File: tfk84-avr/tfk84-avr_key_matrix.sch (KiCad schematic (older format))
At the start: 168 parts

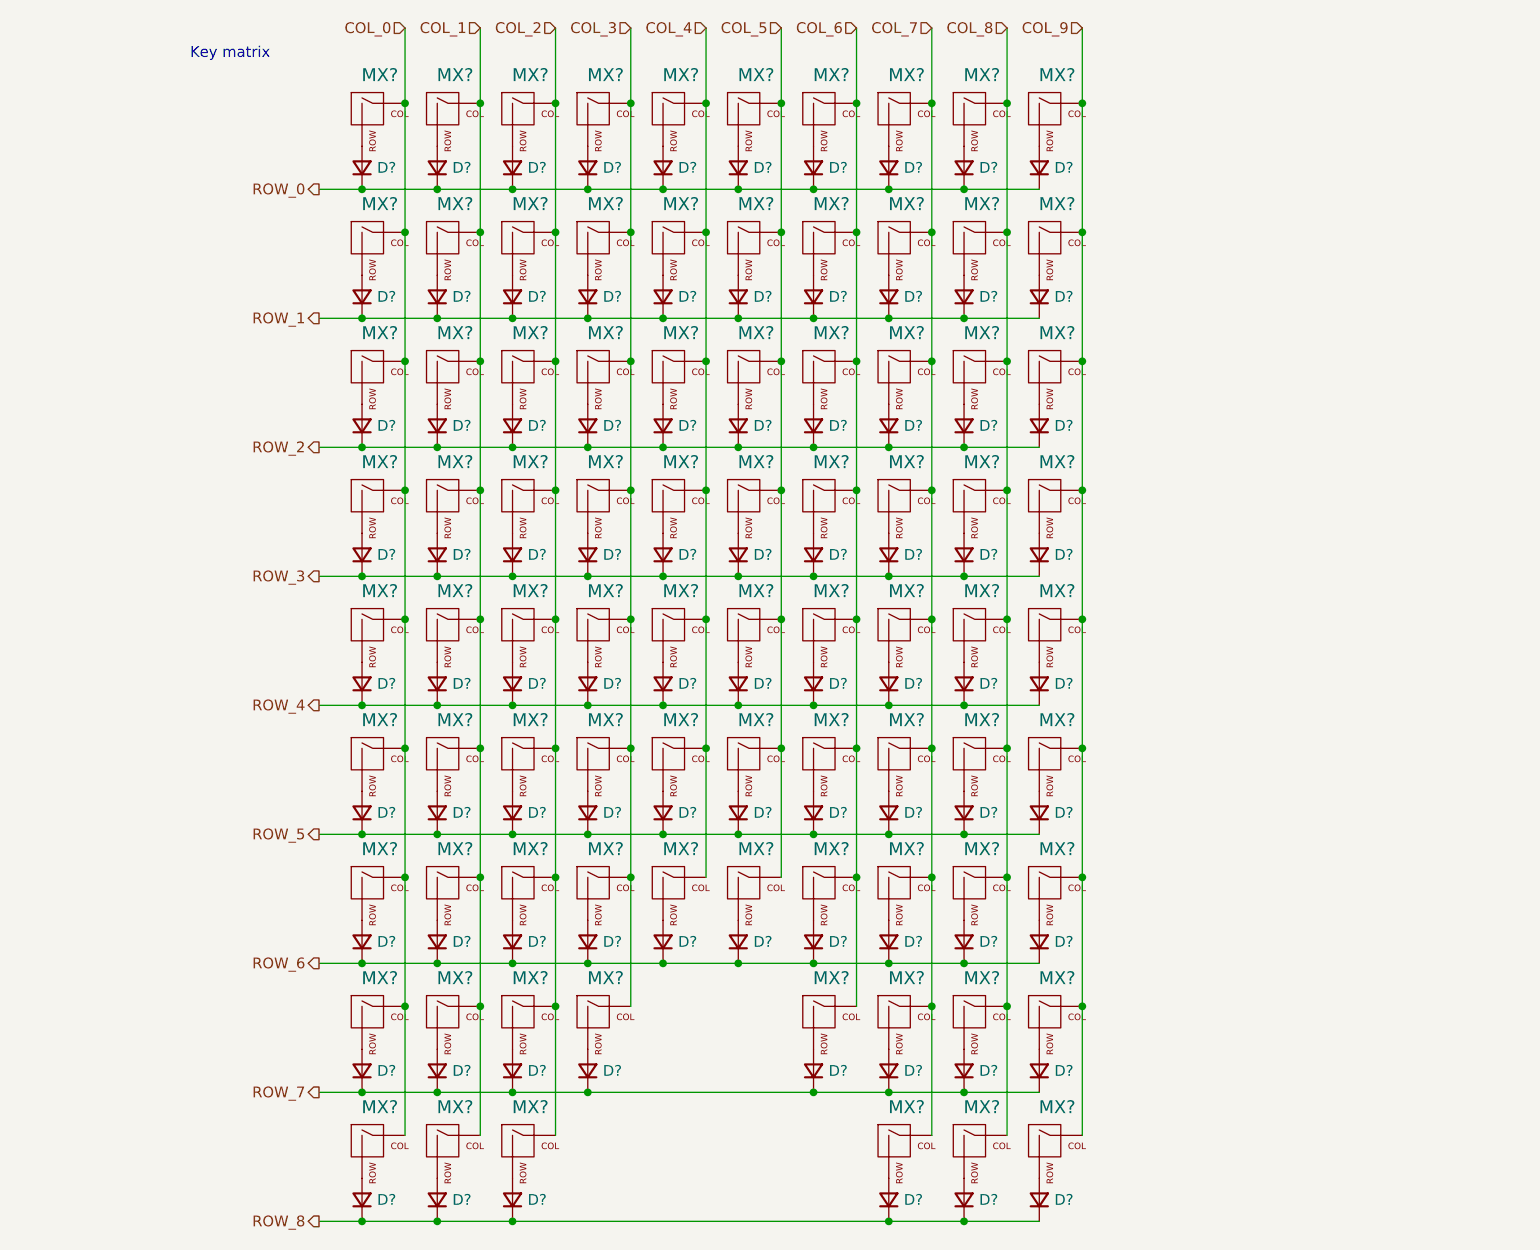
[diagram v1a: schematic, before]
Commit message: Change key matrix to 12x7
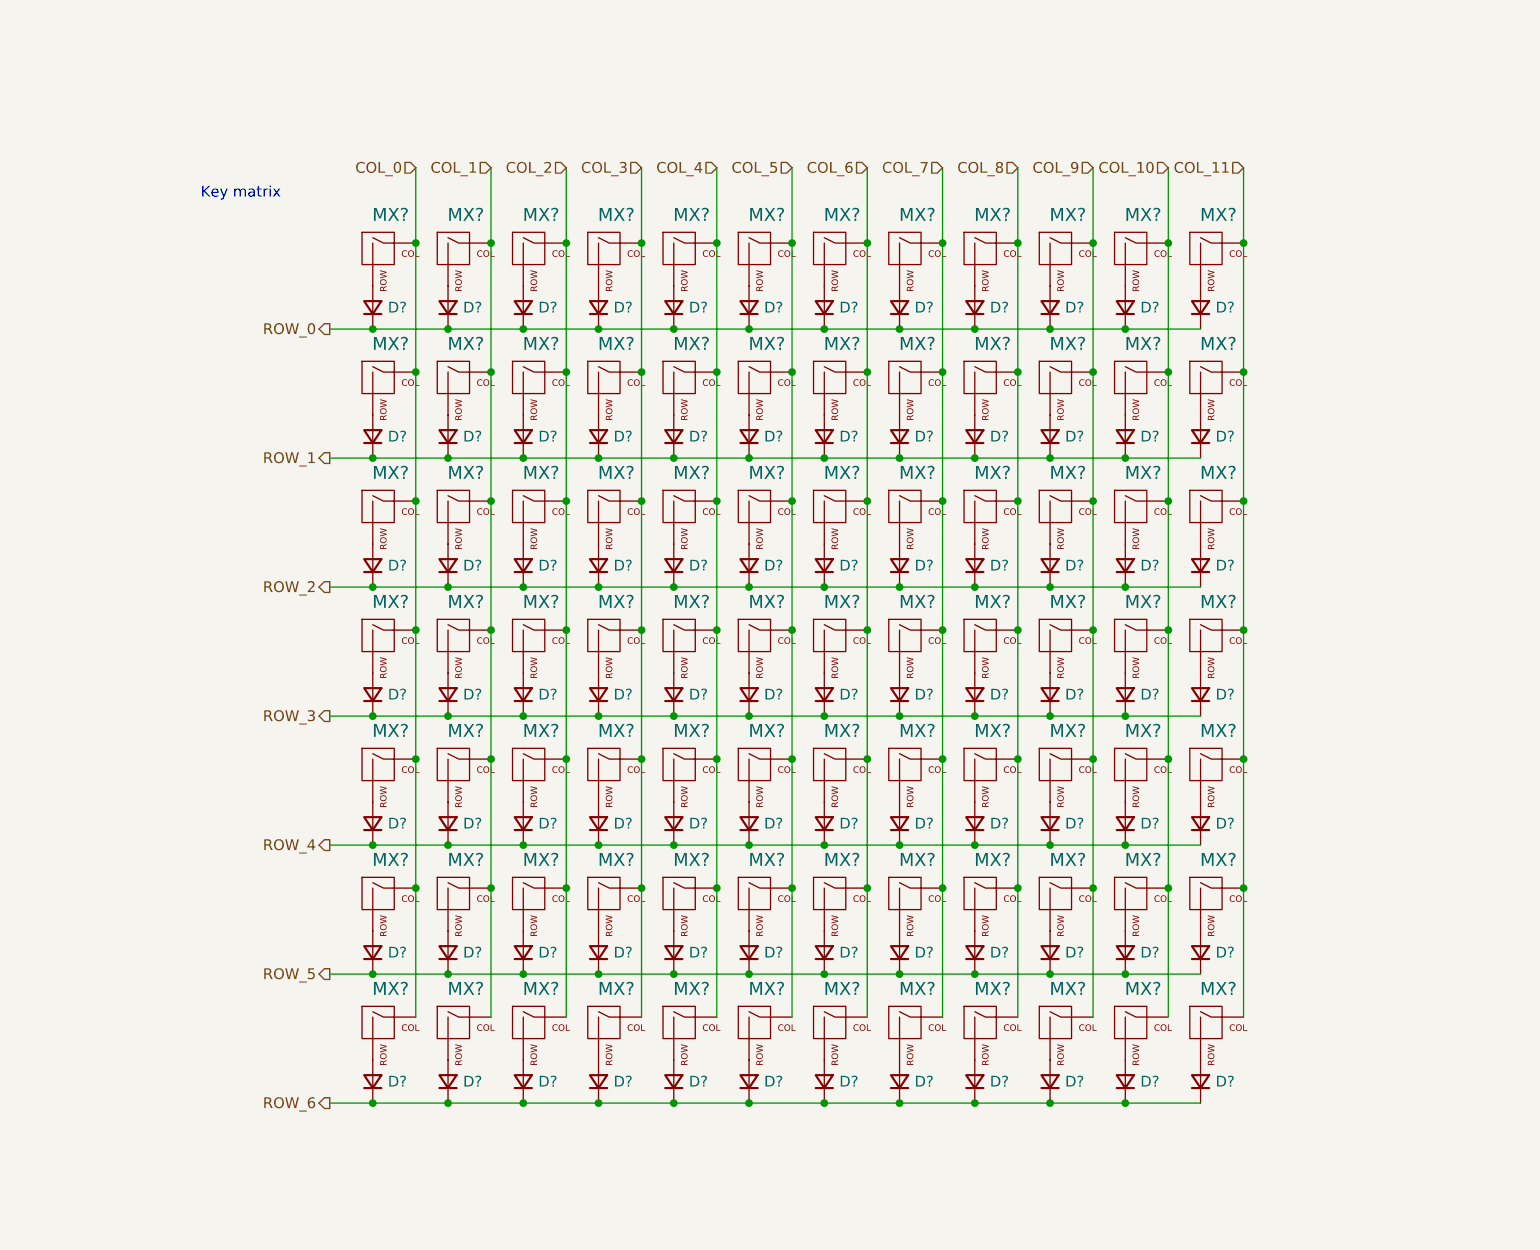
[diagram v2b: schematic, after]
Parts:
- removed D? (x14): D_Small, symbol Device:D_Small
- removed MX? (x14): MX-NoLED, symbol MX_Alps_Hybrid:MX-NoLED
- added D? (x14): D_Small, symbol Device:D_Small
- added MX? (x14): MX-NoLED, symbol MX_Alps_Hybrid:MX-NoLED
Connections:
- net ROW_0: now also D?.1 (K), D?.1 (K)
- net ROW_1: now also D?.1 (K), D?.1 (K)
- net ROW_2: now also D?.1 (K), D?.1 (K)
- net ROW_3: now also D?.1 (K), D?.1 (K)
- net ROW_4: now also D?.1 (K), D?.1 (K)
- net ROW_5: now also D?.1 (K), D?.1 (K)
- net ROW_6: now also D?.1 (K), D?.1 (K)
- new net: D?.2 (A), MX?.2 (ROW) (x14)
- new net COL_10: MX?.1 (COL), MX?.1 (COL), MX?.1 (COL), MX?.1 (COL), MX?.1 (COL), MX?.1 (COL), MX?.1 (COL)
- new net COL_11: MX?.1 (COL), MX?.1 (COL), MX?.1 (COL), MX?.1 (COL), MX?.1 (COL), MX?.1 (COL), MX?.1 (COL)
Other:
- moved on the sheet: D?, MX?

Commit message: Continue schematic
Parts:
- added H?: LShift stabilizer, symbol Mechanical:MountingHole
- added H?: Enter stabilizer, symbol Mechanical:MountingHole
- added H?: Backspace stabilizer, symbol Mechanical:MountingHole
- added H?: Space stabilizer, symbol Mechanical:MountingHole
- gave numbers to parts that had none: 168

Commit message: Begin PCB
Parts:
- D100, D101, D102, D103, D104, D105, D106, D107, D108, D109, D110, D111, D112, D113, D114, D115, D116, D117, D118, D119, D120, D121, D122, D123, D124, D125, D126, D127, D128, D129, D130, D131, D132, D133, D134, D135, D136, D137, D138, D139, D140, D141, D142, D143, D144, D145, D146, D147, D148, D149, D150, D151, D152, D153, D154, D155, D156, D157, D158, D159, D160, D161, D162, D163, D164, D165, D166, D167, D168, D169, D170, D171, D172, D173, D174, D175, D176, D177, D178, D179, D180, D181, D182, D183: footprint (none) -> Diode_SMD:D_SOD-123
- H5, H6, H7: renamed from H?; footprint (none) -> Mounting_Keyboard_Stabilizer:Stabilizer_Cherry_MX_2u_CrtYd
- H8: renamed from H?; footprint (none) -> Mounting_Keyboard_Stabilizer:Stabilizer_Cherry_MX_6.25u
- MX1, MX10, MX11, MX12, MX14, MX15, MX16, MX17, MX18, MX19, MX2, MX20, MX21, MX24, MX26, MX27, MX28, MX29, MX3, MX30, MX31, MX32, MX33, MX34, MX36, MX38, MX39, MX4, MX40, MX41, MX42, MX43, MX44, MX45, MX46, MX47, MX48, MX5, MX50, MX51, MX52, MX53, MX54, MX55, MX56, MX57, MX58, MX6, MX60, MX62, MX63, MX64, MX65, MX66, MX67, MX68, MX69, MX7, MX70, MX71, MX72, MX74, MX75, MX76, MX78, MX79, MX8, MX80, MX81, MX82, MX83, MX84, MX9: footprint (none) -> Switch_Keyboard_Kailh:SW_Hotswap_Kailh_1.00u_NoFrontSilk
- MX13, MX23: footprint (none) -> Switch_Keyboard_Kailh:SW_Hotswap_Kailh_1.50u
- MX22: footprint (none) -> Switch_Keyboard_Kailh:SW_Hotswap_Kailh_2.00u_NoFrontSilk
- MX25, MX59: footprint (none) -> Switch_Keyboard_Kailh:SW_Hotswap_Kailh_1.75u
- MX35, MX37: footprint (none) -> Switch_Keyboard_Kailh:SW_Hotswap_Kailh_2.25u
- MX49, MX61, MX73: footprint (none) -> Switch_Keyboard_Kailh:SW_Hotswap_Kailh_1.25u
- MX77: footprint (none) -> Switch_Keyboard_Kailh:SW_Hotswap_Kailh_6.25u
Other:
- moved on the sheet: H7, H8

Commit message: Add mounting holes for XD84 and KBD75V2 cases
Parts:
- renumbered H5 to H18, H6 to H19, H7 to H20, H8 to H21
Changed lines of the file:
@@
 P 3400 3550
 AR Path="/610B766F" Ref="H?"  Part="1"
-AR Path="/601C3315/610B766F" Ref="H7"  Part="1"
-F 0 "H7" H 3300 3504 50  0000 R CNN
+AR Path="/601C3315/610B766F" Ref="H20"  Part="1"
+F 0 "H20" H 3300 3504 50  0000 R CNN
 F 1 "LShift stabilizer" H 3300 3595 50  0000 R CNN
 F 2 "Mounting_Keyboard_Stabilizer:Stabilizer_Cherry_MX_2u_CrtYd" H 3400 3550 50  0001 C CNN
@@
 P 8400 2950
 AR Path="/610B7675" Ref="H?"  Part="1"
-AR Path="/601C3315/610B7675" Ref="H6"  Part="1"
-F 0 "H6" H 8500 2996 50  0000 L CNN
+AR Path="/601C3315/610B7675" Ref="H19"  Part="1"
+F 0 "H19" H 8500 2996 50  0000 L CNN
 F 1 "Enter stabilizer" H 8500 2905 50  0000 L CNN
 F 2 "Mounting_Keyboard_Stabilizer:Stabilizer_Cherry_MX_2u_CrtYd" H 8400 2950 50  0001 C CNN
@@
 P 8400 2350
 AR Path="/610B767B" Ref="H?"  Part="1"
-AR Path="/601C3315/610B767B" Ref="H5"  Part="1"
-F 0 "H5" H 8500 2396 50  0000 L CNN
+AR Path="/601C3315/610B767B" Ref="H18"  Part="1"
+F 0 "H18" H 8500 2396 50  0000 L CNN
 F 1 "Backspace stabilizer" H 8500 2305 50  0000 L CNN
 F 2 "Mounting_Keyboard_Stabilizer:Stabilizer_Cherry_MX_2u_CrtYd" H 8400 2350 50  0001 C CNN
@@
 P 5550 6000
 AR Path="/610B7681" Ref="H?"  Part="1"
-AR Path="/601C3315/610B7681" Ref="H8"  Part="1"
-F 0 "H8" H 5650 6046 50  0000 L CNN
+AR Path="/601C3315/610B7681" Ref="H21"  Part="1"
+F 0 "H21" H 5650 6046 50  0000 L CNN
 F 1 "Space stabilizer" H 5650 5955 50  0000 L CNN
 F 2 "Mounting_Keyboard_Stabilizer:Stabilizer_Cherry_MX_6.25u" H 5550 6000 50  0001 C CNN

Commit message: Tweak holes
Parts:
- MX14: footprint Switch_Keyboard_Kailh:SW_Hotswap_Kailh_1.00u_NoFrontSilk -> random-keyboard-parts:SW_Hotswap_Kailh_1.00u_NoFrontSilk_CornerPad_TightCrtYd
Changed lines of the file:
@@
 F 0 "MX14" H 4533 2581 60  0000 C CNN
 F 1 "MX-NoLED" H 4533 2549 20  0001 C CNN
-F 2 "Switch_Keyboard_Kailh:SW_Hotswap_Kailh_1.00u_NoFrontSilk" H 3875 2375 60  0001 C CNN
+F 2 "random-keyboard-parts:SW_Hotswap_Kailh_1.00u_NoFrontSilk_CornerPad_TightCrtYd" H 3875 2375 60  0001 C CNN
 F 3 "" H 3875 2375 60  0001 C CNN
 	1    4500 2400

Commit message: Layout switch diodes
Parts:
- MX10, MX17, MX19, MX38, MX53, MX55, MX62, MX71: footprint Switch_Keyboard_Kailh:SW_Hotswap_Kailh_1.00u_NoFrontSilk -> Switch_Keyboard_Kailh:SW_Hotswap_Kailh_1.00u_NoFrontSilk_CornerPad
- MX13: footprint Switch_Keyboard_Kailh:SW_Hotswap_Kailh_1.50u -> Switch_Keyboard_Kailh:SW_Hotswap_Kailh_1.50u_NoFrontSilk_CornerPad
- MX14: footprint random-keyboard-parts:SW_Hotswap_Kailh_1.00u_NoFrontSilk_CornerPad_TightCrtYd -> Switch_Keyboard_Kailh:SW_Hotswap_Kailh_1.00u_NoFrontSilk_CornerPad
- MX23: footprint Switch_Keyboard_Kailh:SW_Hotswap_Kailh_1.50u -> Switch_Keyboard_Kailh:SW_Hotswap_Kailh_1.50u_NoFrontSilk
- MX25, MX59: footprint Switch_Keyboard_Kailh:SW_Hotswap_Kailh_1.75u -> Switch_Keyboard_Kailh:SW_Hotswap_Kailh_1.75u_NoFrontSilk
- MX35, MX37: footprint Switch_Keyboard_Kailh:SW_Hotswap_Kailh_2.25u -> Switch_Keyboard_Kailh:SW_Hotswap_Kailh_2.25u_NoFrontSilk
- MX49, MX61, MX73: footprint Switch_Keyboard_Kailh:SW_Hotswap_Kailh_1.25u -> Switch_Keyboard_Kailh:SW_Hotswap_Kailh_1.25u_NoFrontSilk
- MX77: footprint Switch_Keyboard_Kailh:SW_Hotswap_Kailh_6.25u -> Switch_Keyboard_Kailh:SW_Hotswap_Kailh_6.25u_NoFrontSilk
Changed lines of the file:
@@
 F 0 "MX13" H 4183 2581 60  0000 C CNN
 F 1 "MX-NoLED" H 4183 2549 20  0001 C CNN
-F 2 "Switch_Keyboard_Kailh:SW_Hotswap_Kailh_1.50u" H 3525 2375 60  0001 C CNN
+F 2 "Switch_Keyboard_Kailh:SW_Hotswap_Kailh_1.50u_NoFrontSilk_CornerPad" H 3525 2375 60  0001 C CNN
 F 3 "" H 3525 2375 60  0001 C CNN
 	1    4150 2400
@@
 F 0 "MX25" H 4183 3181 60  0000 C CNN
 F 1 "MX-NoLED" H 4183 3149 20  0001 C CNN
-F 2 "Switch_Keyboard_Kailh:SW_Hotswap_Kailh_1.75u" H 3525 2975 60  0001 C CNN
+F 2 "Switch_Keyboard_Kailh:SW_Hotswap_Kailh_1.75u_NoFrontSilk" H 3525 2975 60  0001 C CNN
 F 3 "" H 3525 2975 60  0001 C CNN
 	1    4150 3000
@@
 F 0 "MX37" H 4183 3781 60  0000 C CNN
 F 1 "MX-NoLED" H 4183 3749 20  0001 C CNN
-F 2 "Switch_Keyboard_Kailh:SW_Hotswap_Kailh_2.25u" H 3525 3575 60  0001 C CNN
+F 2 "Switch_Keyboard_Kailh:SW_Hotswap_Kailh_2.25u_NoFrontSilk" H 3525 3575 60  0001 C CNN
 F 3 "" H 3525 3575 60  0001 C CNN
 	1    4150 3600
@@
 F 0 "MX49" H 4183 4381 60  0000 C CNN
 F 1 "MX-NoLED" H 4183 4349 20  0001 C CNN
-F 2 "Switch_Keyboard_Kailh:SW_Hotswap_Kailh_1.25u" H 3525 4175 60  0001 C CNN
+F 2 "Switch_Keyboard_Kailh:SW_Hotswap_Kailh_1.25u_NoFrontSilk" H 3525 4175 60  0001 C CNN
 F 3 "" H 3525 4175 60  0001 C CNN
 	1    4150 4200
@@
 F 0 "MX61" H 4183 4981 60  0000 C CNN
 F 1 "MX-NoLED" H 4183 4949 20  0001 C CNN
-F 2 "Switch_Keyboard_Kailh:SW_Hotswap_Kailh_1.25u" H 3525 4775 60  0001 C CNN
+F 2 "Switch_Keyboard_Kailh:SW_Hotswap_Kailh_1.25u_NoFrontSilk" H 3525 4775 60  0001 C CNN
 F 3 "" H 3525 4775 60  0001 C CNN
 	1    4150 4800
@@
 F 0 "MX73" H 4183 5581 60  0000 C CNN
 F 1 "MX-NoLED" H 4183 5549 20  0001 C CNN
-F 2 "Switch_Keyboard_Kailh:SW_Hotswap_Kailh_1.25u" H 3525 5375 60  0001 C CNN
+F 2 "Switch_Keyboard_Kailh:SW_Hotswap_Kailh_1.25u_NoFrontSilk" H 3525 5375 60  0001 C CNN
 F 3 "" H 3525 5375 60  0001 C CNN
 	1    4150 5400
@@
 F 0 "MX14" H 4533 2581 60  0000 C CNN
 F 1 "MX-NoLED" H 4533 2549 20  0001 C CNN
-F 2 "random-keyboard-parts:SW_Hotswap_Kailh_1.00u_NoFrontSilk_CornerPad_TightCrtYd" H 3875 2375 60  0001 C CNN
+F 2 "Switch_Keyboard_Kailh:SW_Hotswap_Kailh_1.00u_NoFrontSilk_CornerPad" H 3875 2375 60  0001 C CNN
 F 3 "" H 3875 2375 60  0001 C CNN
 	1    4500 2400
@@
 F 0 "MX38" H 4533 3781 60  0000 C CNN
 F 1 "MX-NoLED" H 4533 3749 20  0001 C CNN
-F 2 "Switch_Keyboard_Kailh:SW_Hotswap_Kailh_1.00u_NoFrontSilk" H 3875 3575 60  0001 C CNN
+F 2 "Switch_Keyboard_Kailh:SW_Hotswap_Kailh_1.00u_NoFrontSilk_CornerPad" H 3875 3575 60  0001 C CNN
 F 3 "" H 3875 3575 60  0001 C CNN
 	1    4500 3600
@@
 F 0 "MX62" H 4533 4981 60  0000 C CNN
 F 1 "MX-NoLED" H 4533 4949 20  0001 C CNN
-F 2 "Switch_Keyboard_Kailh:SW_Hotswap_Kailh_1.00u_NoFrontSilk" H 3875 4775 60  0001 C CNN
+F 2 "Switch_Keyboard_Kailh:SW_Hotswap_Kailh_1.00u_NoFrontSilk_CornerPad" H 3875 4775 60  0001 C CNN
 F 3 "" H 3875 4775 60  0001 C CNN
 	1    4500 4800
@@
 F 0 "MX17" H 5583 2581 60  0000 C CNN
 F 1 "MX-NoLED" H 5583 2549 20  0001 C CNN
-F 2 "Switch_Keyboard_Kailh:SW_Hotswap_Kailh_1.00u_NoFrontSilk" H 4925 2375 60  0001 C CNN
+F 2 "Switch_Keyboard_Kailh:SW_Hotswap_Kailh_1.00u_NoFrontSilk_CornerPad" H 4925 2375 60  0001 C CNN
 F 3 "" H 4925 2375 60  0001 C CNN
 	1    5550 2400
@@
 F 0 "MX53" H 5583 4381 60  0000 C CNN
 F 1 "MX-NoLED" H 5583 4349 20  0001 C CNN
-F 2 "Switch_Keyboard_Kailh:SW_Hotswap_Kailh_1.00u_NoFrontSilk" H 4925 4175 60  0001 C CNN
+F 2 "Switch_Keyboard_Kailh:SW_Hotswap_Kailh_1.00u_NoFrontSilk_CornerPad" H 4925 4175 60  0001 C CNN
 F 3 "" H 4925 4175 60  0001 C CNN
 	1    5550 4200
@@
 F 0 "MX77" H 5583 5581 60  0000 C CNN
 F 1 "MX-NoLED" H 5583 5549 20  0001 C CNN
-F 2 "Switch_Keyboard_Kailh:SW_Hotswap_Kailh_6.25u" H 4925 5375 60  0001 C CNN
+F 2 "Switch_Keyboard_Kailh:SW_Hotswap_Kailh_6.25u_NoFrontSilk" H 4925 5375 60  0001 C CNN
 F 3 "" H 4925 5375 60  0001 C CNN
 	1    5550 5400
@@
 F 0 "MX19" H 6283 2581 60  0000 C CNN
 F 1 "MX-NoLED" H 6283 2549 20  0001 C CNN
-F 2 "Switch_Keyboard_Kailh:SW_Hotswap_Kailh_1.00u_NoFrontSilk" H 5625 2375 60  0001 C CNN
+F 2 "Switch_Keyboard_Kailh:SW_Hotswap_Kailh_1.00u_NoFrontSilk_CornerPad" H 5625 2375 60  0001 C CNN
 F 3 "" H 5625 2375 60  0001 C CNN
 	1    6250 2400
@@
 F 0 "MX55" H 6283 4381 60  0000 C CNN
 F 1 "MX-NoLED" H 6283 4349 20  0001 C CNN
-F 2 "Switch_Keyboard_Kailh:SW_Hotswap_Kailh_1.00u_NoFrontSilk" H 5625 4175 60  0001 C CNN
+F 2 "Switch_Keyboard_Kailh:SW_Hotswap_Kailh_1.00u_NoFrontSilk_CornerPad" H 5625 4175 60  0001 C CNN
 F 3 "" H 5625 4175 60  0001 C CNN
 	1    6250 4200
@@
 F 0 "MX10" H 7333 1981 60  0000 C CNN
 F 1 "MX-NoLED" H 7333 1949 20  0001 C CNN
-F 2 "Switch_Keyboard_Kailh:SW_Hotswap_Kailh_1.00u_NoFrontSilk" H 6675 1775 60  0001 C CNN
+F 2 "Switch_Keyboard_Kailh:SW_Hotswap_Kailh_1.00u_NoFrontSilk_CornerPad" H 6675 1775 60  0001 C CNN
 F 3 "" H 6675 1775 60  0001 C CNN
 	1    7300 1800
@@
 F 0 "MX23" H 7683 2581 60  0000 C CNN
 F 1 "MX-NoLED" H 7683 2549 20  0001 C CNN
-F 2 "Switch_Keyboard_Kailh:SW_Hotswap_Kailh_1.50u" H 7025 2375 60  0001 C CNN
+F 2 "Switch_Keyboard_Kailh:SW_Hotswap_Kailh_1.50u_NoFrontSilk" H 7025 2375 60  0001 C CNN
 F 3 "" H 7025 2375 60  0001 C CNN
 	1    7650 2400
@@
 F 0 "MX35" H 7683 3181 60  0000 C CNN
 F 1 "MX-NoLED" H 7683 3149 20  0001 C CNN
-F 2 "Switch_Keyboard_Kailh:SW_Hotswap_Kailh_2.25u" H 7025 2975 60  0001 C CNN
+F 2 "Switch_Keyboard_Kailh:SW_Hotswap_Kailh_2.25u_NoFrontSilk" H 7025 2975 60  0001 C CNN
 F 3 "" H 7025 2975 60  0001 C CNN
 	1    7650 3000
@@
 F 0 "MX59" H 7683 4381 60  0000 C CNN
 F 1 "MX-NoLED" H 7683 4349 20  0001 C CNN
-F 2 "Switch_Keyboard_Kailh:SW_Hotswap_Kailh_1.75u" H 7025 4175 60  0001 C CNN
+F 2 "Switch_Keyboard_Kailh:SW_Hotswap_Kailh_1.75u_NoFrontSilk" H 7025 4175 60  0001 C CNN
 F 3 "" H 7025 4175 60  0001 C CNN
 	1    7650 4200
@@
 F 0 "MX71" H 7683 4981 60  0000 C CNN
 F 1 "MX-NoLED" H 7683 4949 20  0001 C CNN
-F 2 "Switch_Keyboard_Kailh:SW_Hotswap_Kailh_1.00u_NoFrontSilk" H 7025 4775 60  0001 C CNN
+F 2 "Switch_Keyboard_Kailh:SW_Hotswap_Kailh_1.00u_NoFrontSilk_CornerPad" H 7025 4775 60  0001 C CNN
 F 3 "" H 7025 4775 60  0001 C CNN
 	1    7650 4800
